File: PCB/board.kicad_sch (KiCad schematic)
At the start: 12 parts, among them SW1 SW_SPST, U1 STM32H743VITx

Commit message: working on NRST
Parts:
- added C10: 0.1µF, symbol Device:C
- added R2: 4.7K, symbol Device:R
- added SW2: SW_Push, symbol Switch:SW_Push
- C3: value 100 nF -> 100nF
- C4: value 4.7 µF -> 4.7µF
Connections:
- net GND: now also C10.2, SW2.2
- net VDD_mcu: now also R2.1
- net NRST: now reaches U1.14 (NRST)
- net NRST: now also C10.1, R2.2, SW2.1

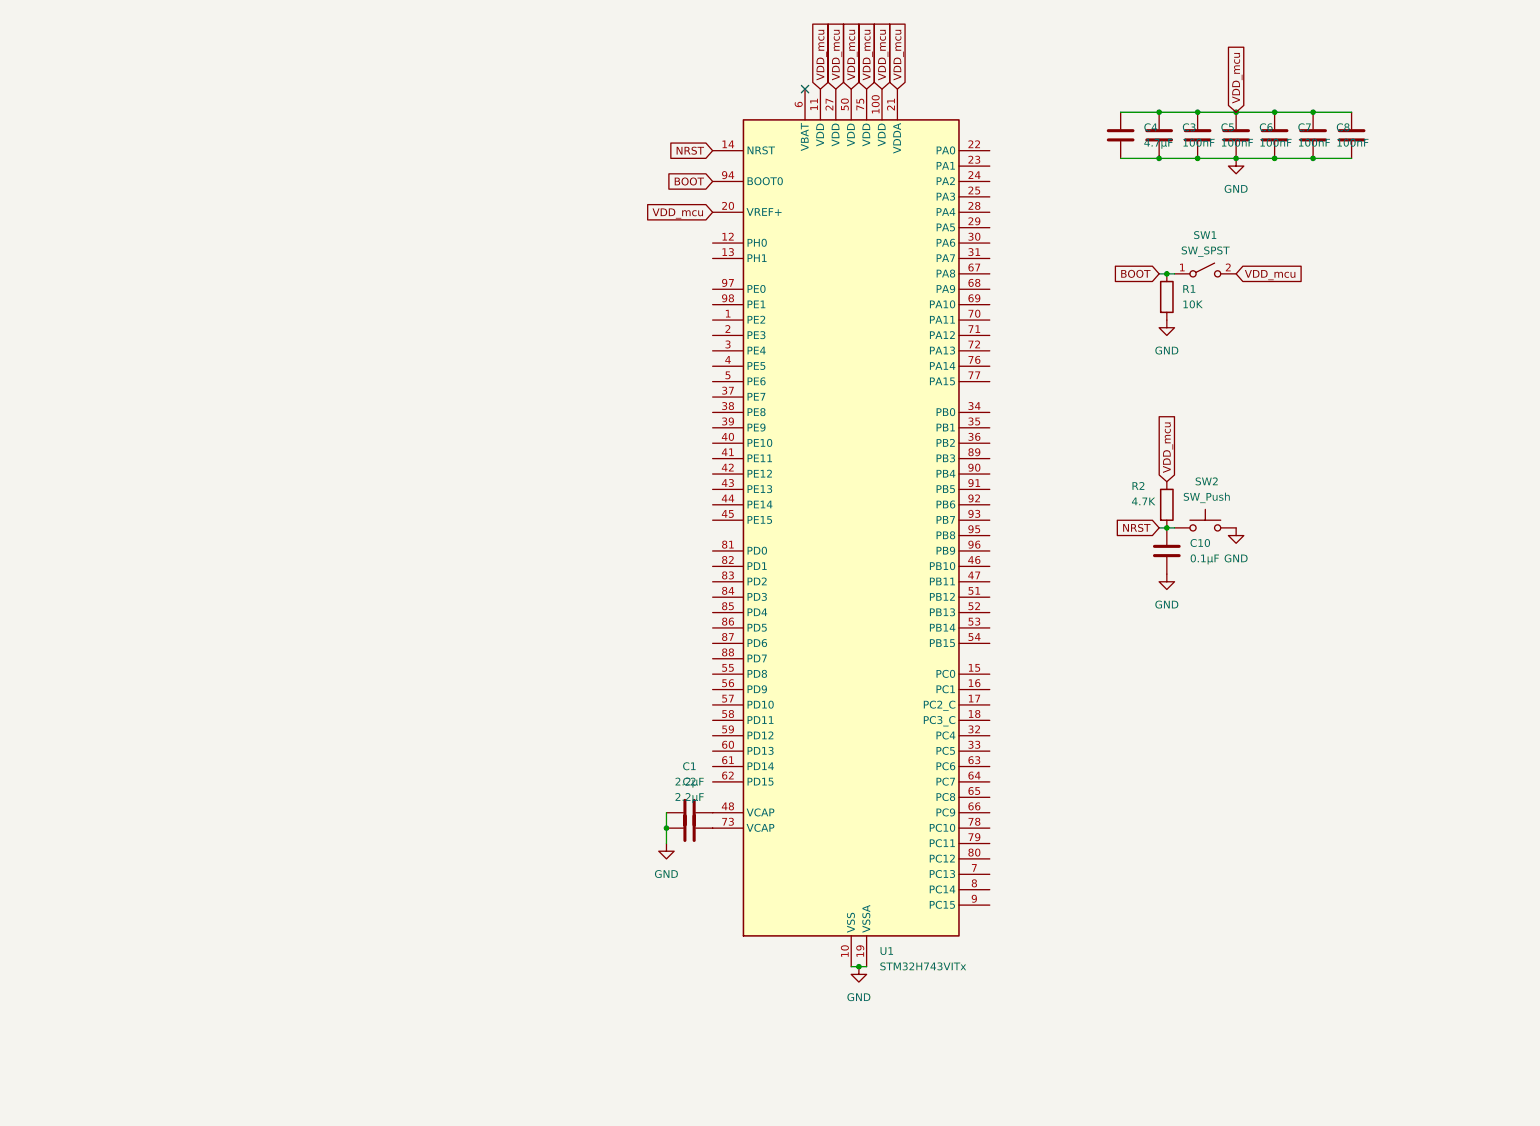
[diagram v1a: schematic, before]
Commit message: separate the boot/reset schematic into a little box!
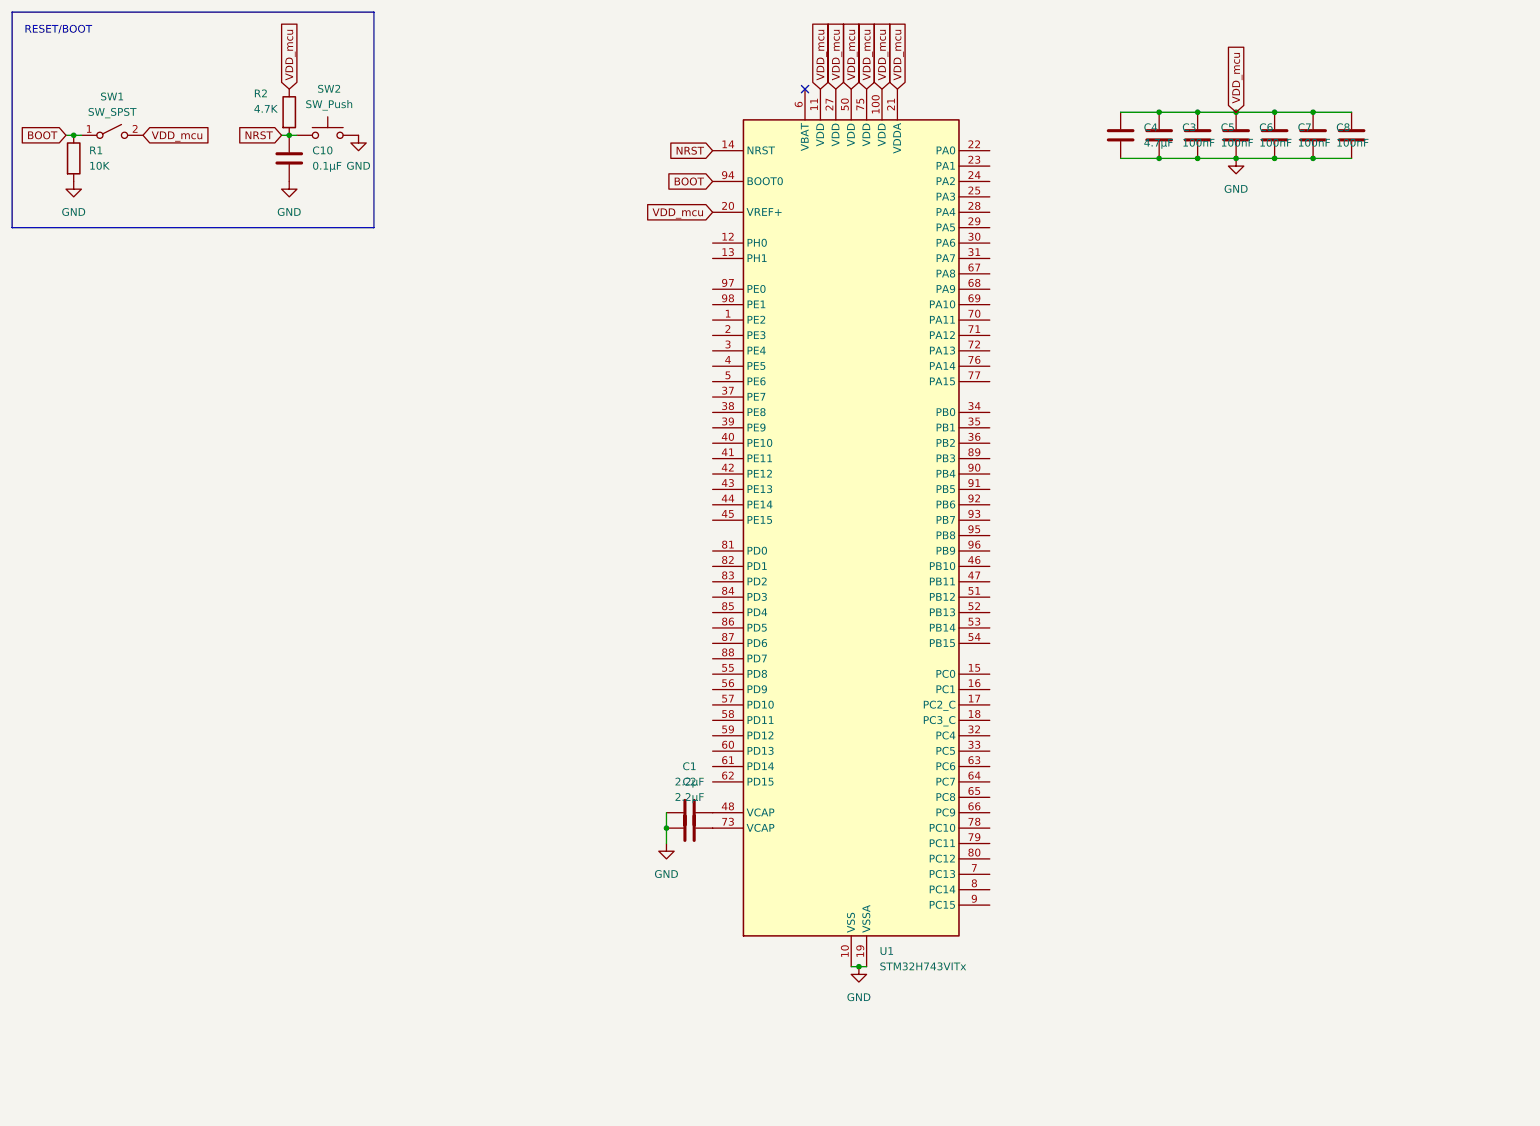
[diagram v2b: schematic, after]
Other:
- note added: "RESET/BOOT"
- moved on the sheet: C10, R1, R2, SW1, SW2
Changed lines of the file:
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@@
 	(generator_version "9.0")
 	(paper "A4")
+	(rectangle
+		(start 12.7 12.7)
+		(end 72.39 48.26)
+		(stroke
+			(width 0)
+			(type default)
+		)
+		(fill
+			(type none)
+		)
+	)
+	(text "RESET/BOOT"
+		(exclude_from_sim no)
+		(at 20.32 15.748 0)
+		(effects
+			(font
+				(size 1.27 1.27)
+			)
+		)
+	)
 	(junction
 		(at 152.4 170.18)
@@
 	)
 	(junction
-		(at 203.2 55.88)
+		(at 22.86 33.02)
 		(diameter 0)
 		(color 0 0 0 0)
@@
 	)
 	(junction
-		(at 203.2 97.79)
+		(at 58.42 33.02)
 		(diameter 0)
 		(color 0 0 0 0)
@@
 	(wire
 		(pts
-			(xy 204.47 55.88) (xy 203.2 55.88)
+			(xy 24.13 33.02) (xy 22.86 33.02)
 		)
 		(stroke
@@
 	(wire
 		(pts
-			(xy 201.93 55.88) (xy 203.2 55.88)
+			(xy 21.59 33.02) (xy 22.86 33.02)
 		)
 		(stroke
@@
 	(wire
 		(pts
-			(xy 201.93 97.79) (xy 203.2 97.79)
+			(xy 57.15 33.02) (xy 58.42 33.02)
 		)
 		(stroke
@@
 	(wire
 		(pts
-			(xy 203.2 97.79) (xy 204.47 97.79)
+			(xy 58.42 33.02) (xy 59.69 33.02)
 		)
 		(stroke
@@
 	(global_label "VDD_mcu"
 		(shape input)
-		(at 203.2 90.17 90)
+		(at 58.42 25.4 90)
 		(fields_autoplaced yes)
 		(effects
@@
 		)
 		(property "Intersheetrefs" "${INTERSHEET_REFS}"
-			(at 203.2 78.6577 90)
+			(at 58.42 13.8877 90)
 			(effects
 				(font
@@
 	(global_label "NRST"
 		(shape input)
-		(at 201.93 97.79 180)
+		(at 57.15 33.02 180)
 		(fields_autoplaced yes)
 		(effects
@@
 		)
 		(property "Intersheetrefs" "${INTERSHEET_REFS}"
-			(at 194.1672 97.79 0)
+			(at 49.3872 33.02 0)
 			(effects
 				(font
@@
 	(global_label "BOOT"
 		(shape input)
-		(at 201.93 55.88 180)
+		(at 21.59 33.02 180)
 		(fields_autoplaced yes)
 		(effects
@@
 		)
 		(property "Intersheetrefs" "${INTERSHEET_REFS}"
-			(at 194.0462 55.88 0)
+			(at 13.7062 33.02 0)
 			(effects
 				(font
@@
 	(global_label "VDD_mcu"
 		(shape input)
-		(at 214.63 55.88 0)
+		(at 34.29 33.02 0)
 		(fields_autoplaced yes)
 		(effects
@@
 		)
 		(property "Intersheetrefs" "${INTERSHEET_REFS}"
-			(at 226.1423 55.88 0)
+			(at 45.8023 33.02 0)
 			(effects
 				(font
@@
 	(symbol
 		(lib_id "power:GND")
-		(at 214.63 97.79 0)
+		(at 69.85 33.02 0)
 		(unit 1)
 		(exclude_from_sim no)
@@
 		(fields_autoplaced yes)
 		(property "Reference" "#PWR06"
-			(at 214.63 104.14 0)
+			(at 69.85 39.37 0)
 			(effects
 				(font
@@
 		)
 		(property "Value" "GND"
-			(at 214.63 102.87 0)
+			(at 69.85 38.1 0)
 			(effects
 				(font
@@
 		)
 		(property "Footprint" ""
-			(at 214.63 97.79 0)
+			(at 69.85 33.02 0)
 			(effects
 				(font
@@
 		)
 		(property "Datasheet" ""
-			(at 214.63 97.79 0)
+			(at 69.85 33.02 0)
 			(effects
 				(font
@@
 		)
 		(property "Description" "Power symbol creates a global label with name \"GND\" , ground"
-			(at 214.63 97.79 0)
+			(at 69.85 33.02 0)
 			(effects
 				(font
@@
 	(symbol
 		(lib_id "power:GND")
-		(at 203.2 105.41 0)
+		(at 58.42 40.64 0)
 		(unit 1)
 		(exclude_from_sim no)
@@
 		(fields_autoplaced yes)
 		(property "Reference" "#PWR05"
-			(at 203.2 111.76 0)
+			(at 58.42 46.99 0)
 			(effects
 				(font
@@
 		)
 		(property "Value" "GND"
-			(at 203.2 110.49 0)
+			(at 58.42 45.72 0)
 			(effects
 				(font
@@
 		)
 		(property "Footprint" ""
-			(at 203.2 105.41 0)
+			(at 58.42 40.64 0)
 			(effects
 				(font
@@
 		)
 		(property "Datasheet" ""
-			(at 203.2 105.41 0)
+			(at 58.42 40.64 0)
 			(effects
 				(font
@@
 		)
 		(property "Description" "Power symbol creates a global label with name \"GND\" , ground"
-			(at 203.2 105.41 0)
+			(at 58.42 40.64 0)
 			(effects
 				(font
@@
 	(symbol
 		(lib_id "Switch:SW_SPST")
-		(at 209.55 55.88 0)
+		(at 29.21 33.02 0)
 		(unit 1)
 		(exclude_from_sim no)
@@
 		(fields_autoplaced yes)
 		(property "Reference" "SW1"
-			(at 209.55 49.53 0)
+			(at 29.21 26.67 0)
 			(effects
 				(font
@@
 		)
 		(property "Value" "SW_SPST"
-			(at 209.55 52.07 0)
+			(at 29.21 29.21 0)
 			(effects
 				(font
@@
 		)
 		(property "Footprint" ""
-			(at 209.55 55.88 0)
+			(at 29.21 33.02 0)
 			(effects
 				(font
@@
 		)
 		(property "Datasheet" "~"
-			(at 209.55 55.88 0)
+			(at 29.21 33.02 0)
 			(effects
 				(font
@@
 		)
 		(property "Description" "Single Pole Single Throw (SPST) switch"
-			(at 209.55 55.88 0)
+			(at 29.21 33.02 0)
 			(effects
 				(font
@@
 	(symbol
 		(lib_id "Device:R")
-		(at 203.2 59.69 0)
+		(at 22.86 36.83 0)
 		(unit 1)
 		(exclude_from_sim no)
@@
 		(fields_autoplaced yes)
 		(property "Reference" "R1"
-			(at 205.74 58.4199 0)
+			(at 25.4 35.5599 0)
 			(effects
 				(font
@@
 		)
 		(property "Value" "10K"
-			(at 205.74 60.9599 0)
+			(at 25.4 38.0999 0)
 			(effects
 				(font
@@
 		)
 		(property "Footprint" ""
-			(at 201.422 59.69 90)
+			(at 21.082 36.83 90)
 			(effects
 				(font
@@
 		)
 		(property "Datasheet" "~"
-			(at 203.2 59.69 0)
+			(at 22.86 36.83 0)
 			(effects
 				(font
@@
 		)
 		(property "Description" "Resistor"
-			(at 203.2 59.69 0)
+			(at 22.86 36.83 0)
 			(effects
 				(font
@@
 	(symbol
 		(lib_id "Device:C")
-		(at 203.2 101.6 0)
+		(at 58.42 36.83 0)
 		(unit 1)
 		(exclude_from_sim no)
@@
 		(fields_autoplaced yes)
 		(property "Reference" "C10"
-			(at 207.01 100.3299 0)
+			(at 62.23 35.5599 0)
 			(effects
 				(font
@@
 		)
 		(property "Value" "0.1µF"
-			(at 207.01 102.8699 0)
+			(at 62.23 38.0999 0)
 			(effects
 				(font
@@
 		)
 		(property "Footprint" ""
-			(at 204.1652 105.41 0)
+			(at 59.3852 40.64 0)
 			(effects
 				(font
@@
 		)
 		(property "Datasheet" "~"
-			(at 203.2 101.6 0)
+			(at 58.42 36.83 0)
 			(effects
 				(font
@@
 		)
 		(property "Description" "Unpolarized capacitor"
-			(at 203.2 101.6 0)
+			(at 58.42 36.83 0)
 			(effects
 				(font
@@
 	(symbol
 		(lib_id "Switch:SW_Push")
-		(at 209.55 97.79 0)
+		(at 64.77 33.02 0)
 		(unit 1)
 		(exclude_from_sim no)
@@
 		(dnp no)
 		(property "Reference" "SW2"
-			(at 209.804 90.17 0)
+			(at 65.024 25.4 0)
 			(effects
 				(font
@@
 		)
 		(property "Value" "SW_Push"
-			(at 209.804 92.71 0)
+			(at 65.024 27.94 0)
 			(effects
 				(font
@@
 		)
 		(property "Footprint" ""
-			(at 209.55 92.71 0)
+			(at 64.77 27.94 0)
 			(effects
 				(font
@@
 		)
 		(property "Datasheet" "~"
-			(at 209.55 92.71 0)
+			(at 64.77 27.94 0)
 			(effects
 				(font
@@
 		)
 		(property "Description" "Push button switch, generic, two pins"
-			(at 209.55 97.79 0)
+			(at 64.77 33.02 0)
 			(effects
 				(font
@@
 	(symbol
 		(lib_id "Device:R")
-		(at 203.2 93.98 0)
+		(at 58.42 29.21 0)
 		(unit 1)
 		(exclude_from_sim no)
@@
 		(dnp no)
 		(property "Reference" "R2"
-			(at 197.358 90.932 0)
+			(at 52.578 26.162 0)
 			(effects
 				(font
@@
 		)
 		(property "Value" "4.7K"
-			(at 197.358 93.472 0)
+			(at 52.578 28.702 0)
 			(effects
 				(font
@@
 		)
 		(property "Footprint" ""
-			(at 201.422 93.98 90)
+			(at 56.642 29.21 90)
 			(effects
 				(font
@@
 		)
 		(property "Datasheet" "~"
-			(at 203.2 93.98 0)
+			(at 58.42 29.21 0)
 			(effects
 				(font
@@
 		)
 		(property "Description" "Resistor"
-			(at 203.2 93.98 0)
+			(at 58.42 29.21 0)
 			(effects
 				(font
@@
 	(symbol
 		(lib_id "power:GND")
-		(at 203.2 63.5 0)
+		(at 22.86 40.64 0)
 		(unit 1)
 		(exclude_from_sim no)
@@
 		(fields_autoplaced yes)
 		(property "Reference" "#PWR04"
-			(at 203.2 69.85 0)
+			(at 22.86 46.99 0)
 			(effects
 				(font
@@
 		)
 		(property "Value" "GND"
-			(at 203.2 68.58 0)
+			(at 22.86 45.72 0)
 			(effects
 				(font
@@
 		)
 		(property "Footprint" ""
-			(at 203.2 63.5 0)
+			(at 22.86 40.64 0)
 			(effects
 				(font
@@
 		)
 		(property "Datasheet" ""
-			(at 203.2 63.5 0)
+			(at 22.86 40.64 0)
 			(effects
 				(font
@@
 		)
 		(property "Description" "Power symbol creates a global label with name \"GND\" , ground"
-			(at 203.2 63.5 0)
-			(effects
-				(font
+			(at 22.86 40.64 0)
+			(effects
+				(font

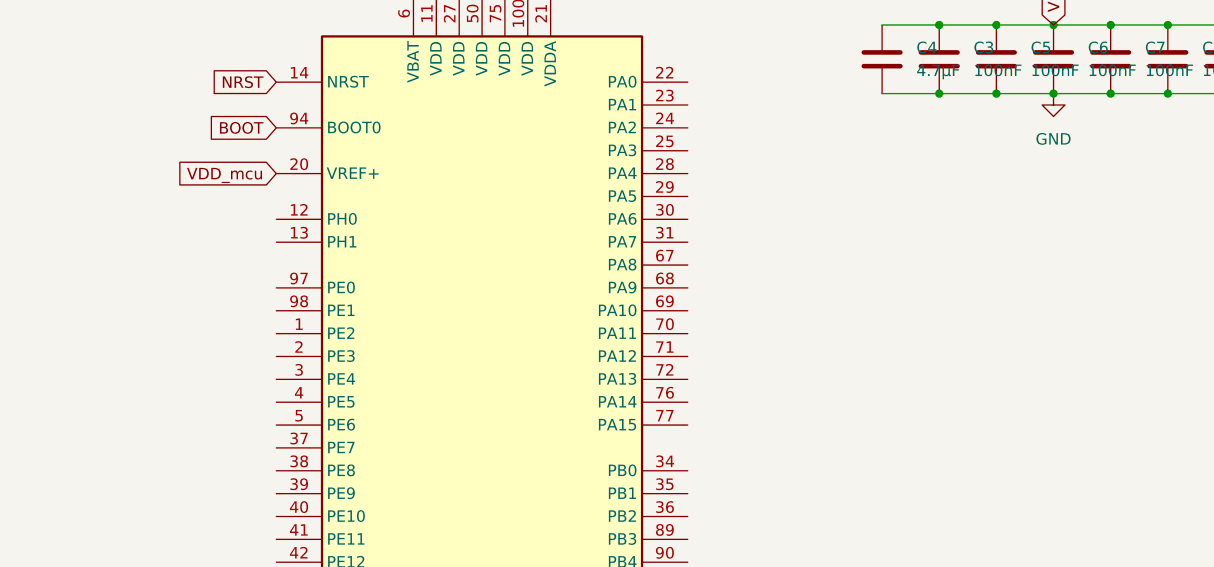
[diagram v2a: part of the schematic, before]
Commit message: added crystal oscillator
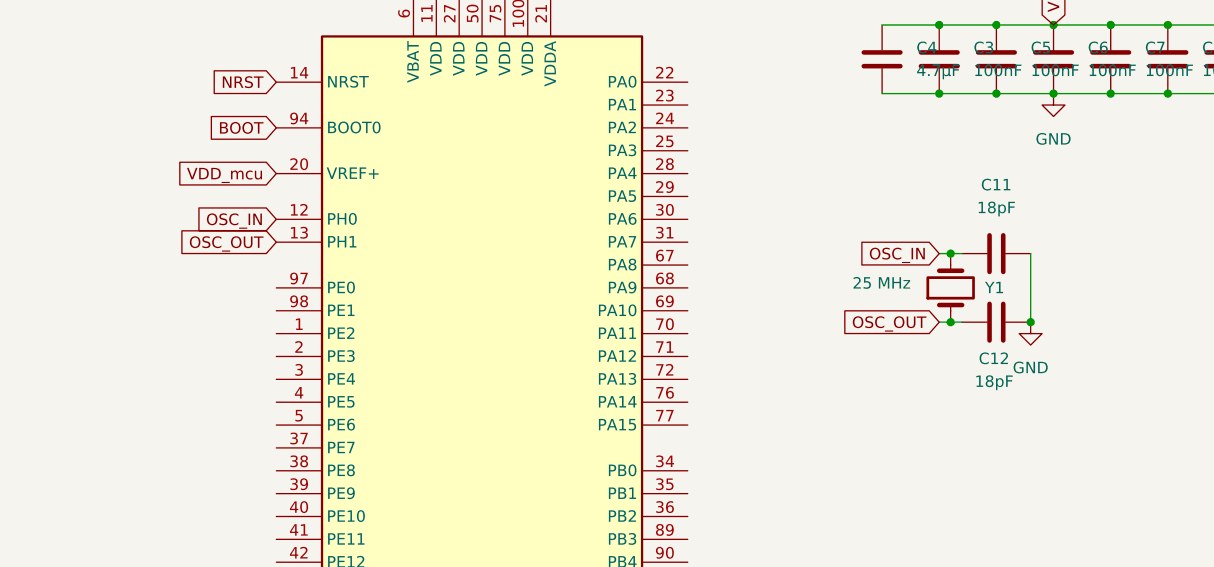
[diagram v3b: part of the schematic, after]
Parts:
- added C11, C12: 18pF, symbol Device:C
- added Y1: 25 MHz, symbol Device:Crystal
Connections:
- net GND: now also C11.2, C12.2
- net OSC_IN: now reaches U1.12 (PH0)
- net OSC_IN: now also C11.1, Y1.2
- net OSC_OUT: now reaches U1.13 (PH1)
- net OSC_OUT: now also C12.1, Y1.1
